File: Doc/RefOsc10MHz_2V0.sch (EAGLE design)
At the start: 70 parts, among them CON11 MCX-J-P-X-RA-SM1, CON2 HEADER-2X5SMD, CON3 1-227161-0, CON4 AVR-ISP-10SMD, CON5 AVR-JTAG-10SMD, IC1 ATmega328-P, IC11 712-RXM-GNSS-TM-B, IC2 LC4032V_XXT44, IC202 CFPT-126, IC3 74HCT221D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

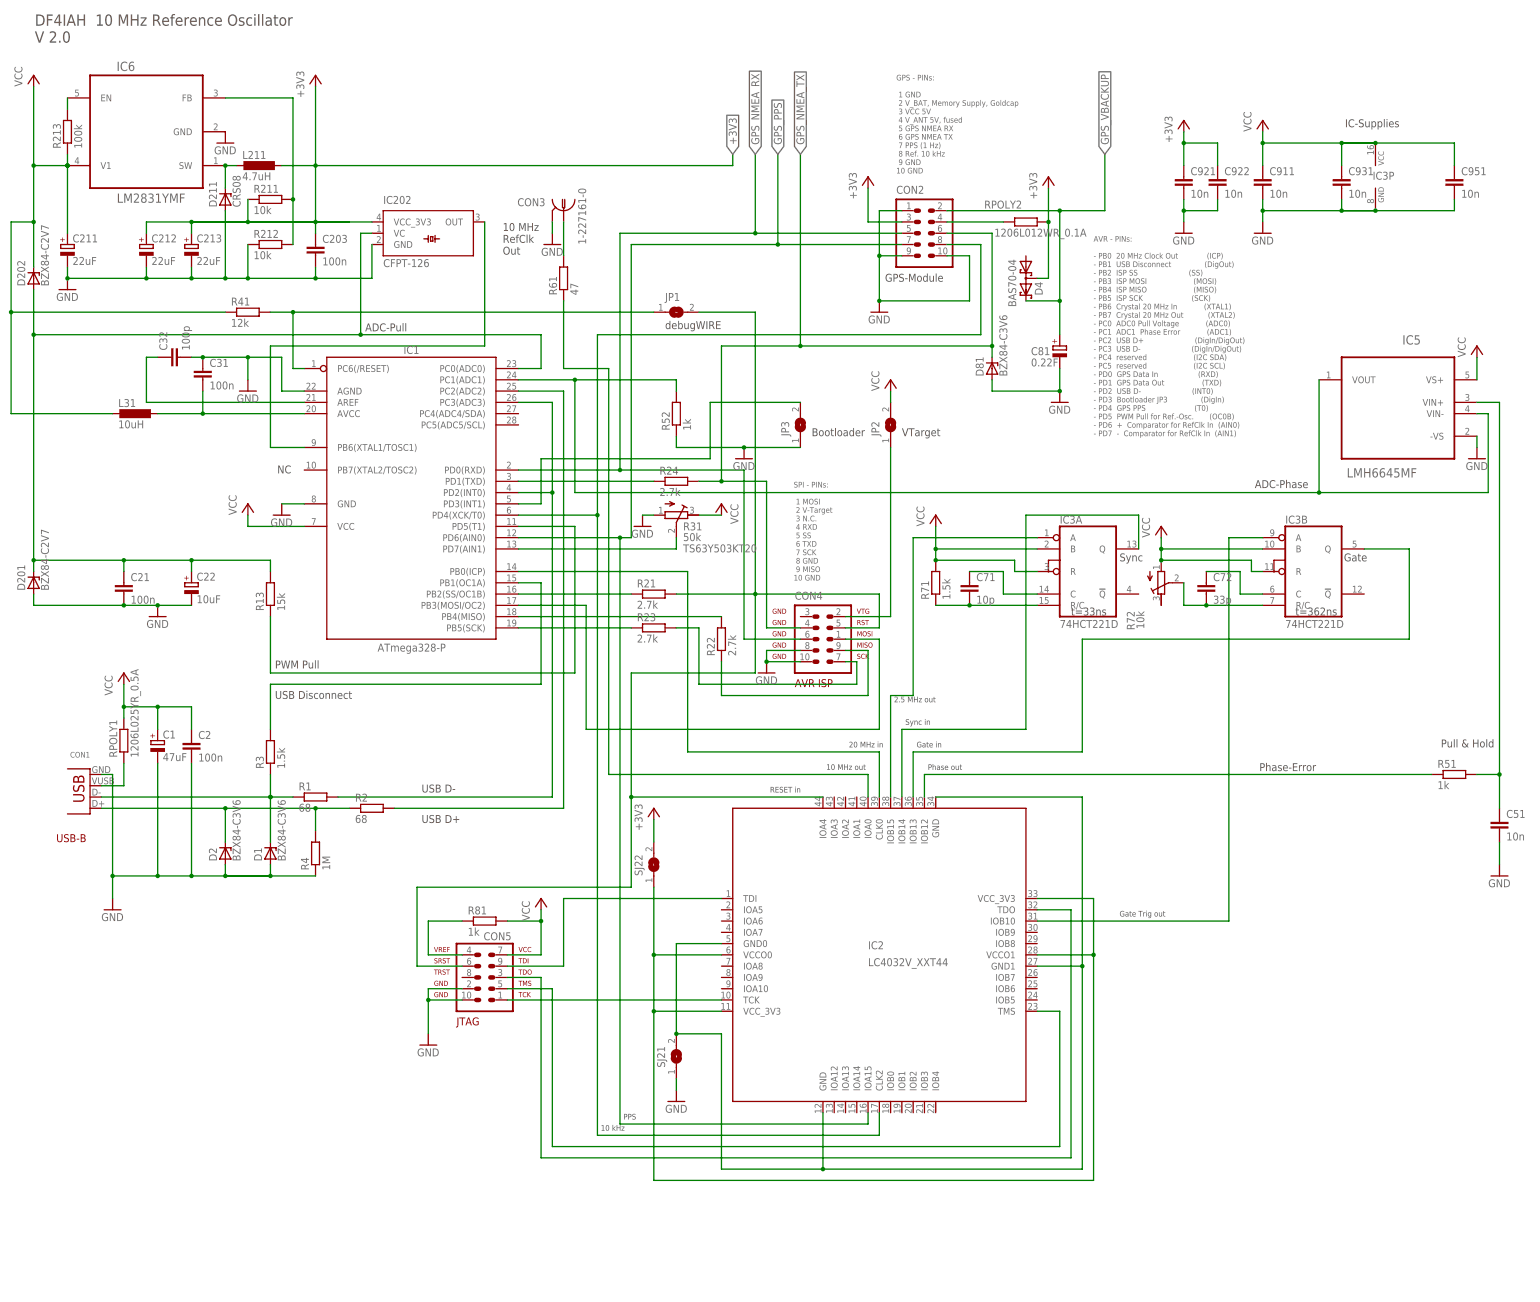
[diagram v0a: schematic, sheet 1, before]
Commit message: avr_DF4IAH_Bootloader - Doc - Eagle: I2C header added
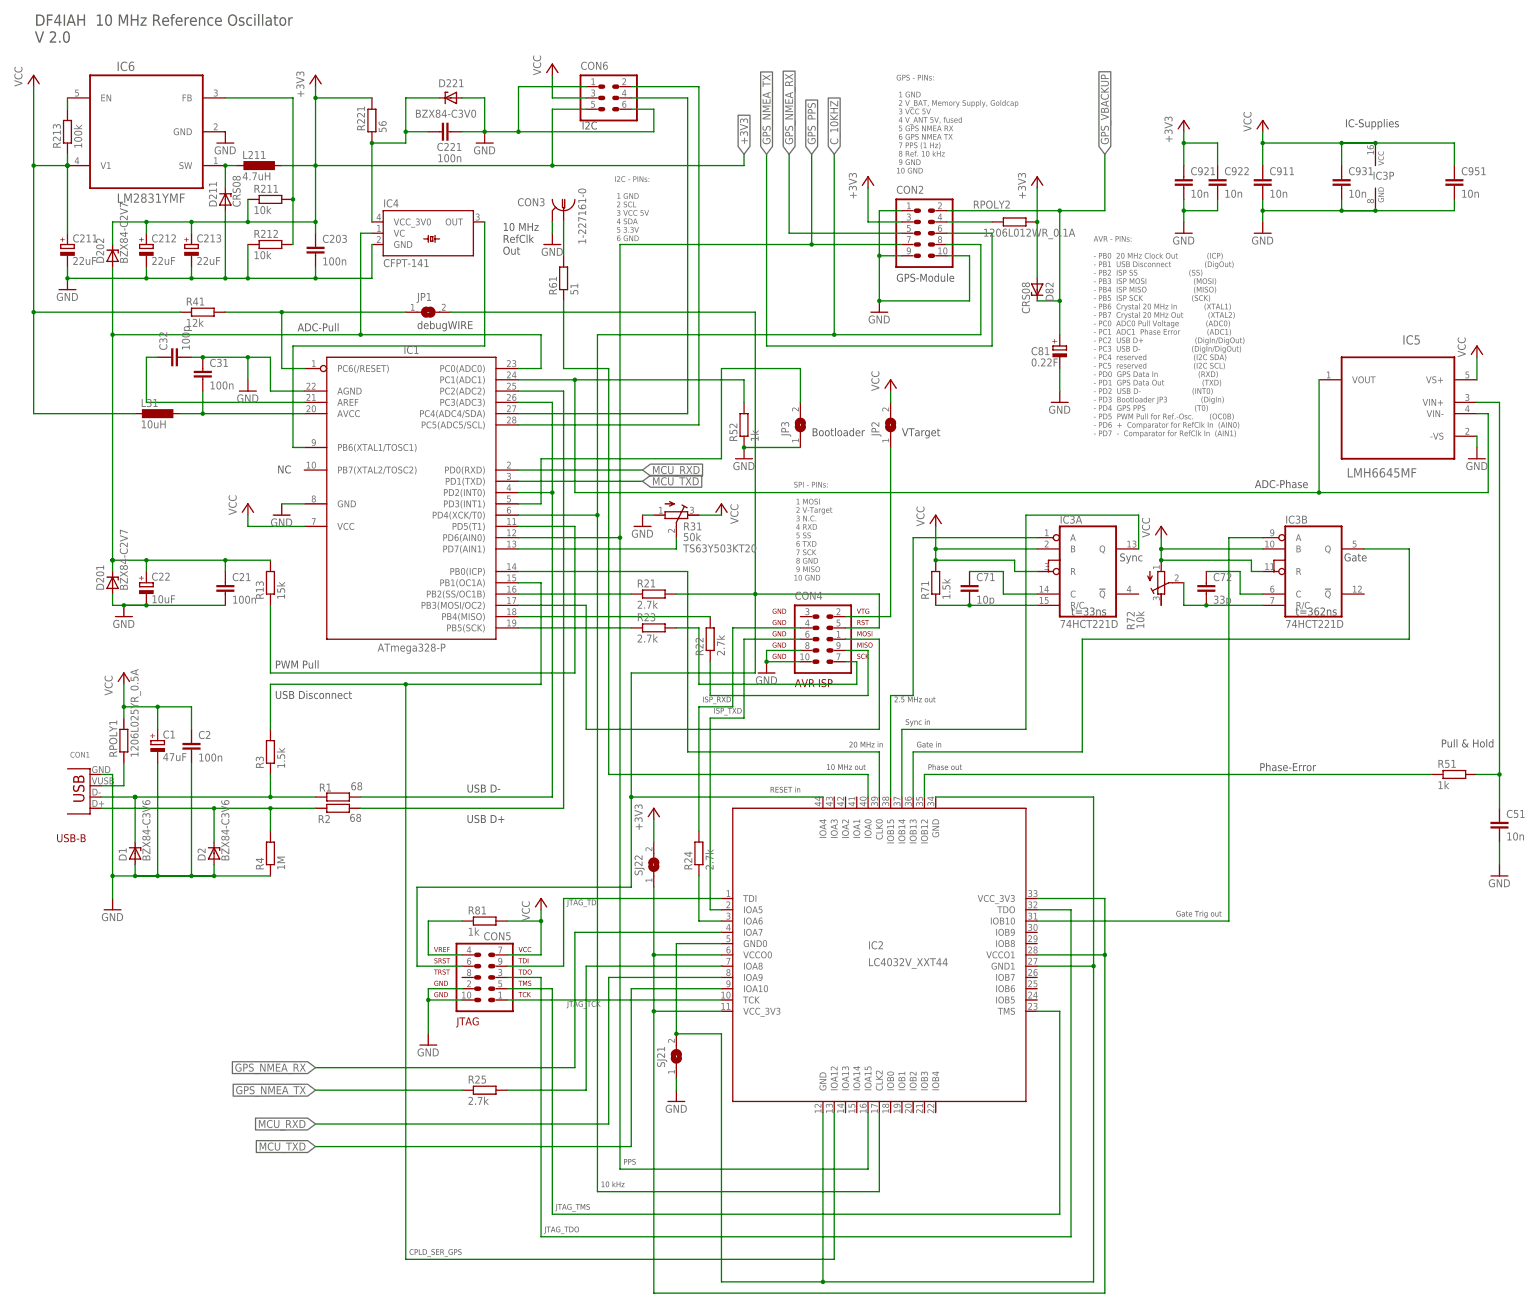
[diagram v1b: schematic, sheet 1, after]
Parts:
- removed D4: BAS70-04, diode:BAS70-04
- removed D81: BZX84-C3V6, diode:BZX84CSMD
- removed IC202: CFPT-126, df4iah:CFPT-126
- added C221: 100n, rcl:C-EUC0805
- added CON6: HEADER-2X3SMD, df4iah:HEADER-2X3SMD
- added D221: BZX84-C3V0, diode:BZX84CSMD
- added D82: CRS08, diode:ZENER-DIODESOT23
- added IC4: CFPT-141, df4iah:CFPT-141
- added R221: 56, rcl:R-EU_R0805
- added R25: 2.7k, rcl:R-EU_R0805
- R61: value 47 -> 51
- renumbered C1101 to C111, LFP1101 to LFP111
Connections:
- removed net TXD: IC1.PD1(TXD), R24.1
- new net +3V0: C221.1, D221.C, IC4.VCC_3V0, R221.2
- new net CPLD_GPS_NMEA_TX: IC2.IOA8, R25.2
- new net CPLD_ISP_RXD: IC2.IOA6, R24.1
- new net ISP_RXD: CON4.4, R24.2
- new net ISP_TXD: CON4.6, IC2.IOA5
- new net MCU_RXD: IC1.PD0(RXD), IC2.IOA9
- new net MCU_TXD: IC1.PD1(TXD), IC2.IOA10
- new net N$1: CON6.2, IC1.PC5(ADC5/SCL)
- new net N$3: CON6.4, IC1.PC4(ADC4/SDA)
- net +3V3: now also CON6.5, D202.C, D82.A, R221.1; no longer D4.C1A2, IC202.VCC_3V3
- net GND: now also C221.2, CON6.1, CON6.6, D221.A, IC4.GND; no longer D81.A, IC202.GND
- net GPS_NMEA_RX: now also IC2.IOA7; no longer CON4.6, IC1.PD0(RXD)
- net GPS_NMEA_TX: now also R25.1; no longer CON4.4, D81.C, R24.2
- net GPS_VBACKUP: now also D82.C; no longer D4.C2
- net N_ADC_PULL: now also IC4.VC; no longer IC202.VC
- net N_USB_DISC: now also IC2.IOA12
- net TOSC1: now also IC4.OUT; no longer IC202.OUT
- net VCC: now also CON6.3; no longer D202.C
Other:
- note added: "CPLD_SER_GPS"
- note added: "I2C"
- note added: "I2C - PINs: 1 GND 2 SCL 3 VCC 5V 4 SDA 5 3.3V 6 GND"
- note added: "ISP_RXD"
- note added: "ISP_TXD"
- note added: "JTAG_TCK"
- note added: "JTAG_TDI"
- note added: "JTAG_TDO"
- note added: "JTAG_TMS"
- moved on the sheet: C21, C22, D1, D2, D201, D202, JP1, L31, R1, R13, R2, R22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

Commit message: avr_DF4IAH_Bootloader - Doc - Eagle: USB-B and BNC connectors changed
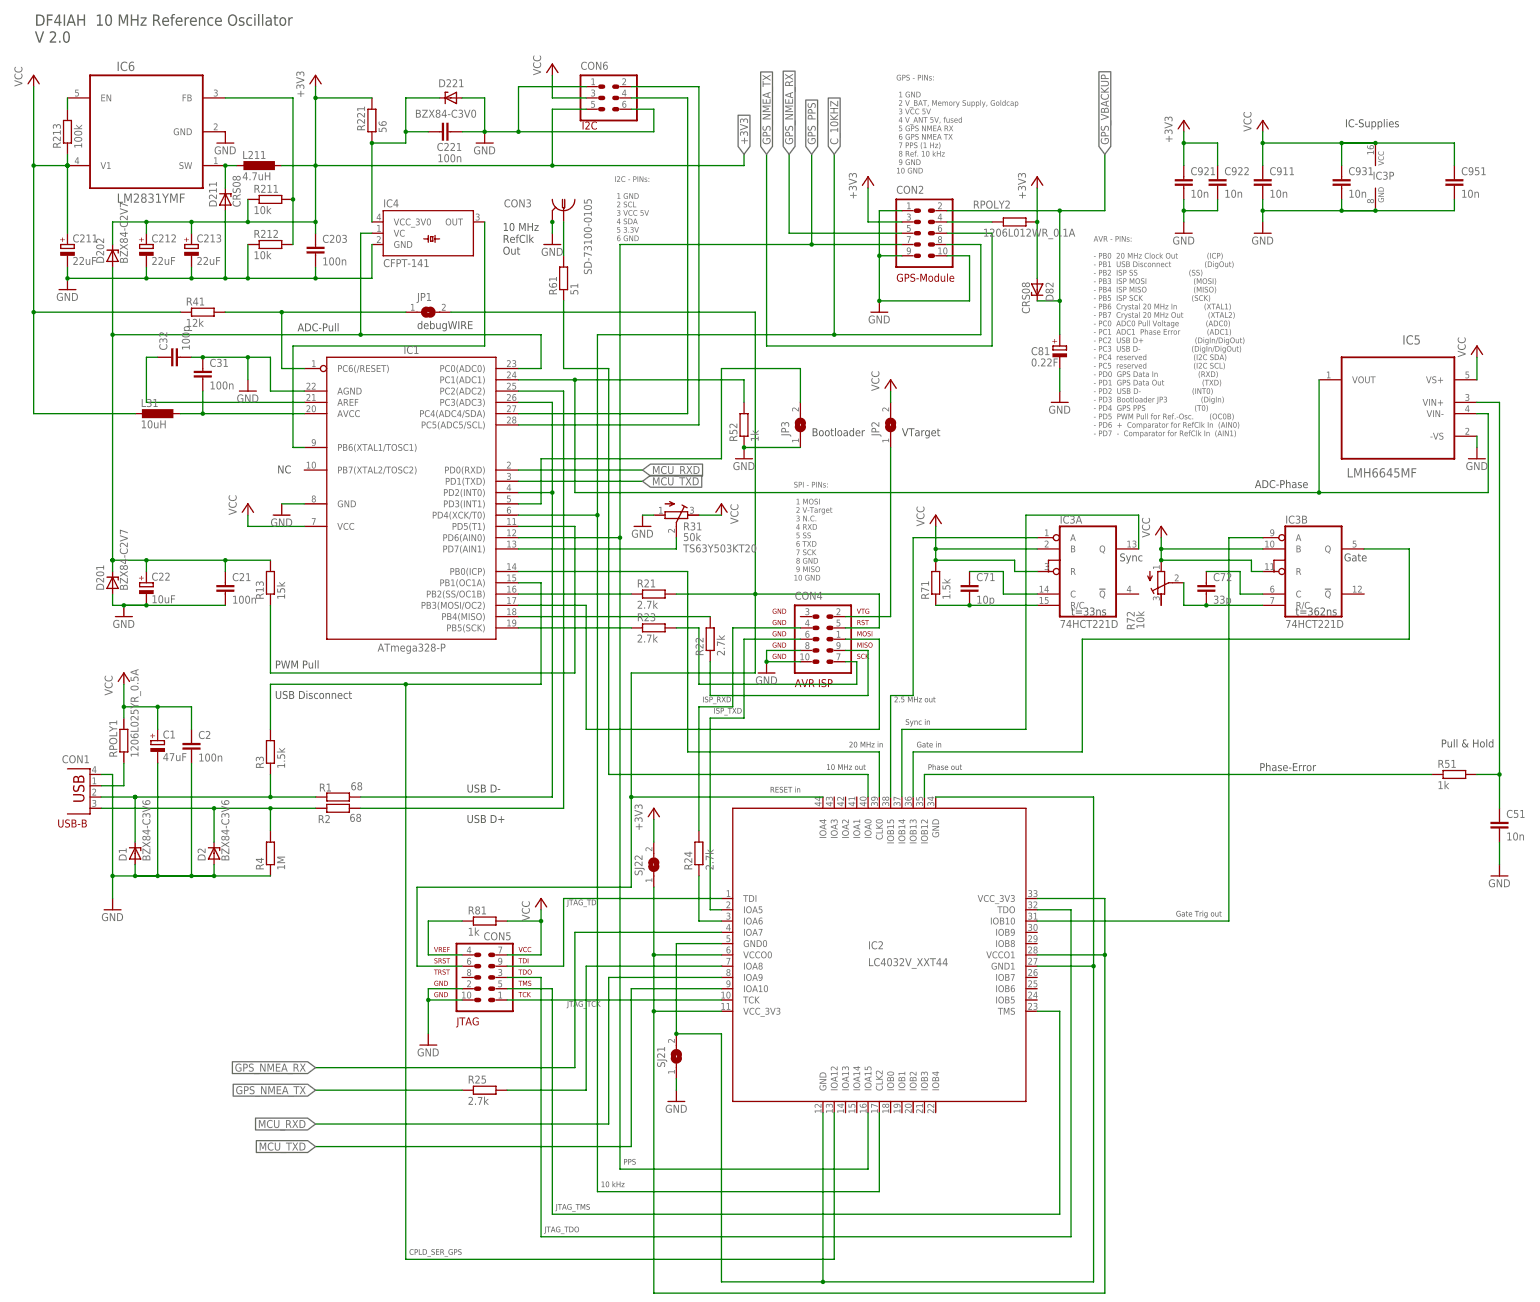
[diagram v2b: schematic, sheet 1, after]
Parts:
- CON1: value (none) -> TYCO-AMP_USBUSB-B_SMT; device con-usb-3:USB-B-S -> df4iah:TYCO-AMP_USBUSB-B_SMT
- CON3: value 1-227161-0 -> SD-73100-0105; device con-coax:1-227161-0 -> df4iah:MOLEX_BNC-JACK-50R_SD-73100-0105
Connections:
- net GND: now also CON3.3
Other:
- moved on the sheet: CON1
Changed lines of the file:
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@@
 <part name="GND15" library="supply1" deviceset="GND" device=""/>
 <part name="P+9" library="supply1" deviceset="VCC" device=""/>
-<part name="CON3" library="con-coax" deviceset="?227161*" device="1-" technology="-0"/>
 <part name="GND9" library="supply1" deviceset="GND" device=""/>
 <part name="GND18" library="supply1" deviceset="GND" device=""/>
@@
 <part name="GND21" library="supply1" deviceset="GND" device=""/>
 <part name="P+7" library="supply1" deviceset="VCC" device=""/>
-<part name="CON1" library="con-usb-3" deviceset="USB" device="-B-S"/>
 <part name="RAHMEN1" library="e-elektro-zeichnungsrahmen" deviceset="RAHMEN_A4_8Z-19S_OHNE_DOKUMENTENFELD" device=""/>
 <part name="IC11" library="df4iah" deviceset="712-RXM-GNSS-TM-B" device=""/>
@@
 <part name="CON6" library="df4iah" deviceset="HEADER-2X3" device="SMD"/>
 <part name="P+8" library="supply1" deviceset="VCC" device=""/>
+<part name="CON3" library="df4iah" deviceset="MOLEX_BNC-JACK-50R_SD-73100-0105" device="" value="SD-73100-0105"/>
+<part name="CON1" library="df4iah" deviceset="TYCO-AMP_USB" device="USB-B_SMT"/>
 </parts>
 <sheets>
@@
 <text x="205.74" y="170.18" size="1.778" layer="97">VTarget</text>
 <text x="96.52" y="194.31" size="1.778" layer="97">debugWIRE</text>
-<text x="15.24" y="78.74" size="1.778" layer="94">USB-B</text>
+<text x="15.494" y="82.042" size="1.778" layer="94">USB-B</text>
 <text x="248.92" y="170.18" size="1.27" layer="96" font="fixed">AVR - PINs:
 - PB0  20 MHz Clock Out             (ICP)
@@
 <text x="286.258" y="94.742" size="1.778" layer="97">Phase-Error</text>
 <text x="305.308" y="141.986" size="1.778" layer="97">Gate</text>
-<text x="204.47" y="204.978" size="1.778" layer="97">GPS-Module</text>
+<text x="204.47" y="204.978" size="1.778" layer="94">GPS-Module</text>
 <text x="204.47" y="229.362" size="1.27" layer="96" font="fixed">GPS - PINs:
  1 GND
@@
  5 3.3V
  6 GND</text>
-<text x="133.604" y="239.268" size="1.778" layer="97">I2C</text>
+<text x="133.604" y="239.268" size="1.778" layer="94">I2C</text>
 </plain>
 <instances>
@@
 <instance part="GND15" gate="1" x="287.02" y="215.9"/>
 <instance part="P+9" gate="VCC" x="287.02" y="241.3"/>
-<instance part="CON3" gate="G$1" x="129.54" y="220.98" smashed="yes" rot="R270">
-<attribute name="VALUE" x="134.62" y="213.36" size="1.778" layer="96" rot="R90"/>
-<attribute name="NAME" x="119.126" y="221.996" size="1.778" layer="95"/>
-</instance>
 <instance part="GND9" gate="1" x="127" y="213.36"/>
 <instance part="GND18" gate="1" x="200.66" y="198.12"/>
@@
 <instance part="GND21" gate="1" x="335.28" y="165.1"/>
 <instance part="P+7" gate="VCC" x="335.28" y="190.5"/>
-<instance part="CON1" gate="G$1" x="22.86" y="93.98" rot="R180"/>
 <instance part="+3V5" gate="G$1" x="198.12" y="228.6"/>
 <instance part="+3V6" gate="G$1" x="236.22" y="228.6"/>
@@
 <instance part="CON6" gate="G$1" x="139.7" y="246.38"/>
 <instance part="P+8" gate="VCC" x="127" y="254"/>
+<instance part="CON3" gate="G$1" x="129.54" y="220.98" smashed="yes" rot="R270">
+<attribute name="VALUE" x="134.112" y="223.774" size="1.778" layer="96" rot="R270"/>
+<attribute name="NAME" x="116.078" y="221.742" size="1.778" layer="95"/>
+</instance>
+<instance part="CON1" gate="G$1" x="22.86" y="93.98" smashed="yes" rot="R180">
+<attribute name="NAME" x="16.51" y="96.52" size="1.778" layer="95"/>
+</instance>
 </instances>
 <busses>
@@
 </segment>
 <segment>
-<pinref part="CON3" gate="G$1" pin="2"/>
 <pinref part="GND9" gate="1" pin="GND"/>
 <wire x1="127" y1="218.44" x2="127" y2="215.9" width="0.1524" layer="91"/>
+<pinref part="CON3" gate="G$1" pin="3"/>
+<pinref part="CON3" gate="G$1" pin="2"/>
+<junction x="127" y="218.44"/>
 </segment>
 <segment>
@@
 <pinref part="D1" gate="G$1" pin="A"/>
 <pinref part="D2" gate="G$1" pin="A"/>
-<pinref part="CON1" gate="G$1" pin="GND"/>
 <wire x1="27.94" y1="71.12" x2="27.94" y2="93.98" width="0.1524" layer="91"/>
 <wire x1="27.94" y1="93.98" x2="25.4" y2="93.98" width="0.1524" layer="91"/>
@@
 <pinref part="R4" gate="G$1" pin="1"/>
 <pinref part="C2" gate="G$1" pin="2"/>
+<pinref part="CON1" gate="G$1" pin="GND"/>
 </segment>
 <segment>
@@
 <pinref part="D1" gate="G$1" pin="C"/>
 <wire x1="33.02" y1="88.9" x2="25.4" y2="88.9" width="0.1524" layer="91"/>
-<pinref part="CON1" gate="G$1" pin="D-"/>
 <pinref part="R1" gate="G$1" pin="1"/>
 <pinref part="R3" gate="G$1" pin="1"/>
 <junction x="63.5" y="88.9"/>
+<pinref part="CON1" gate="G$1" pin="D-"/>
 </segment>
 </net>
@@
 <pinref part="D2" gate="G$1" pin="C"/>
 <wire x1="50.8" y1="86.36" x2="25.4" y2="86.36" width="0.1524" layer="91"/>
-<pinref part="CON1" gate="G$1" pin="D+"/>
 <junction x="50.8" y="86.36"/>
 <pinref part="R2" gate="G$1" pin="1"/>
 <pinref part="R4" gate="G$1" pin="2"/>
+<pinref part="CON1" gate="G$1" pin="D+"/>
 </segment>
 </net>
@@
 <net name="N$42" class="0">
 <segment>
-<pinref part="CON3" gate="G$1" pin="1"/>
 <wire x1="129.54" y1="218.44" x2="129.54" y2="210.82" width="0.1524" layer="91"/>
 <pinref part="R61" gate="G$1" pin="2"/>
+<pinref part="CON3" gate="G$1" pin="1"/>
 </segment>
 </net>
@@
 <segment>
 <pinref part="RPOLY1" gate="G$1" pin="1"/>
-<pinref part="CON1" gate="G$1" pin="VBUS"/>
 <wire x1="30.48" y1="96.52" x2="30.48" y2="91.44" width="0.1524" layer="91"/>
 <wire x1="30.48" y1="91.44" x2="25.4" y2="91.44" width="0.1524" layer="91"/>
+<pinref part="CON1" gate="G$1" pin="VBUS"/>
 </segment>
 </net>
@@
 <instances>
 <instance part="RAHMEN1" gate="G$1" x="0" y="7.62"/>
-<instance part="IC11" gate="G$1" x="152.4" y="101.6"/>
+<instance part="IC11" gate="G$1" x="152.4" y="101.6" smashed="yes">
+<attribute name="NAME" x="149.606" y="125.984" size="2.032" layer="95"/>
+</instance>
 <instance part="GND22" gate="1" x="124.46" y="66.04"/>
 <instance part="+3V3" gate="G$1" x="124.46" y="91.44"/>
